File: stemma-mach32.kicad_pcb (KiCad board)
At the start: 2 copper layers, 17.8 x 35.6 mm, 32 parts, among them J1 Conn_01x09_Male, J2 Conn_01x04_Male, J3 Conn_01x04_Male, J4 Conn_01x09_Male, J5 DebugEdge_02x04, Q1 BSS138, Q2 BSS138, U1 AP2112K-3.3, U2 MACHXO2-32QFN

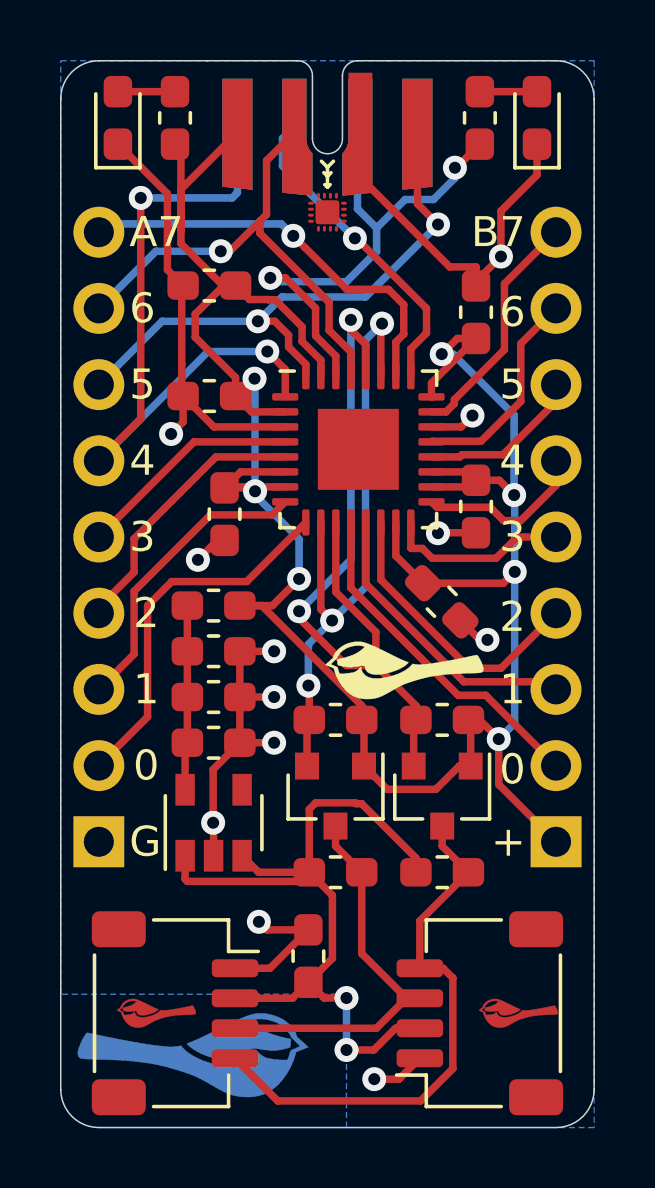
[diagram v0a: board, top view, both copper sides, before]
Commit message: Updates the debug-edge connector
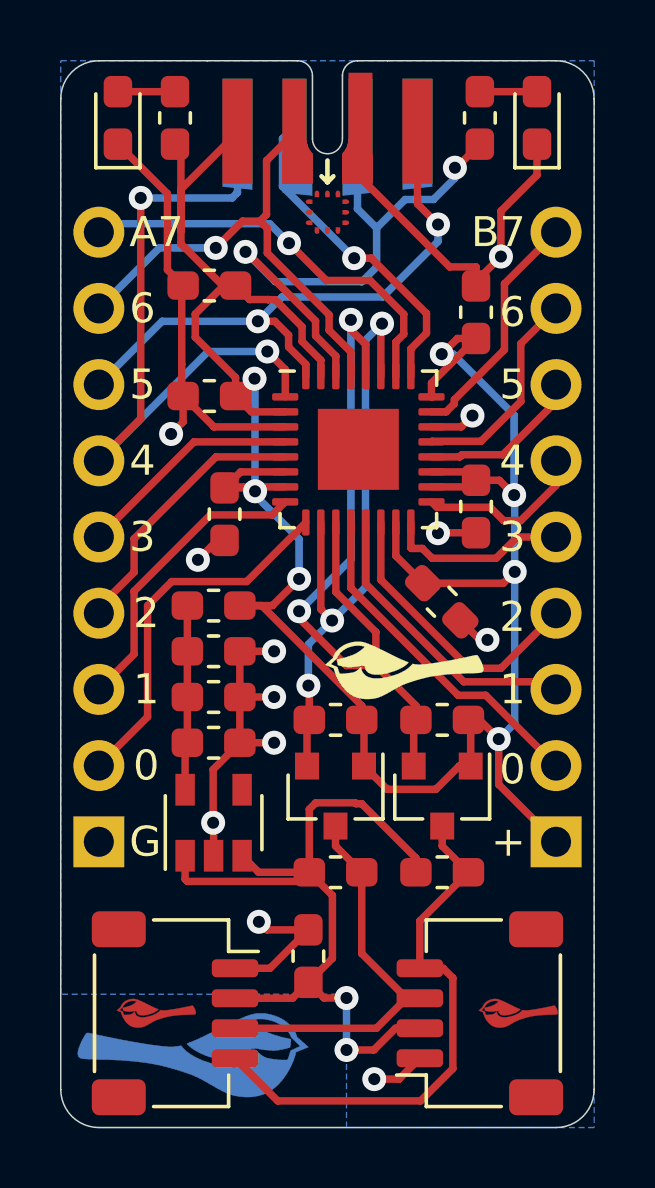
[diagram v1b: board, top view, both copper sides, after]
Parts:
- moved J5 1.00 mm to (133.6, 76.2)
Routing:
- net /TCK: track 17.8 -> 20.2 mm
